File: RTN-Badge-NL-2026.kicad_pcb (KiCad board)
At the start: 2 copper layers, 85.5 x 54 mm, 151 parts, among them J1 USB_A_Edge_Connector, J2 DEBUG, J3 GPIO, SW1 BOOT, SW2 RST, SW3 USER1, SW4 USER2, U1 CH32V203F6P6, U2 XC6206PxxxMR, Y1 8MHz

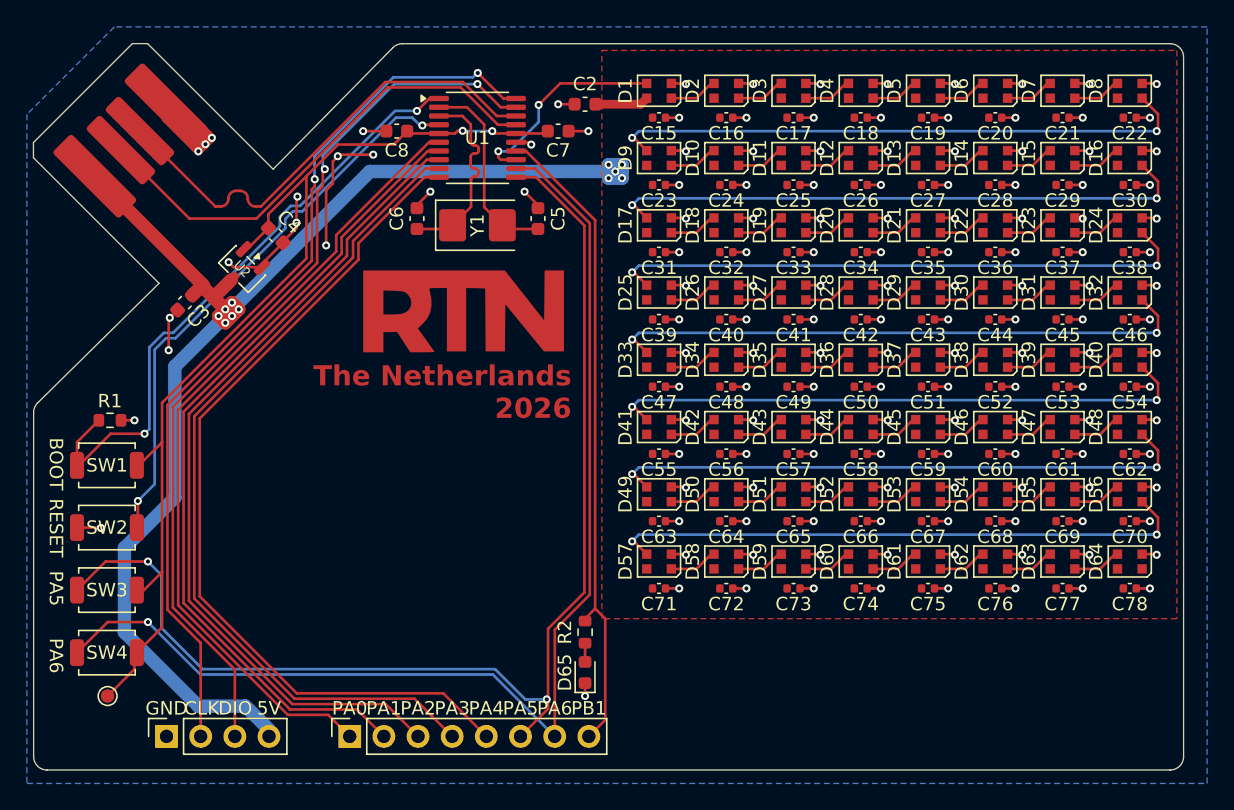
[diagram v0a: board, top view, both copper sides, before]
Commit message: Hide reference designators, clean up traces
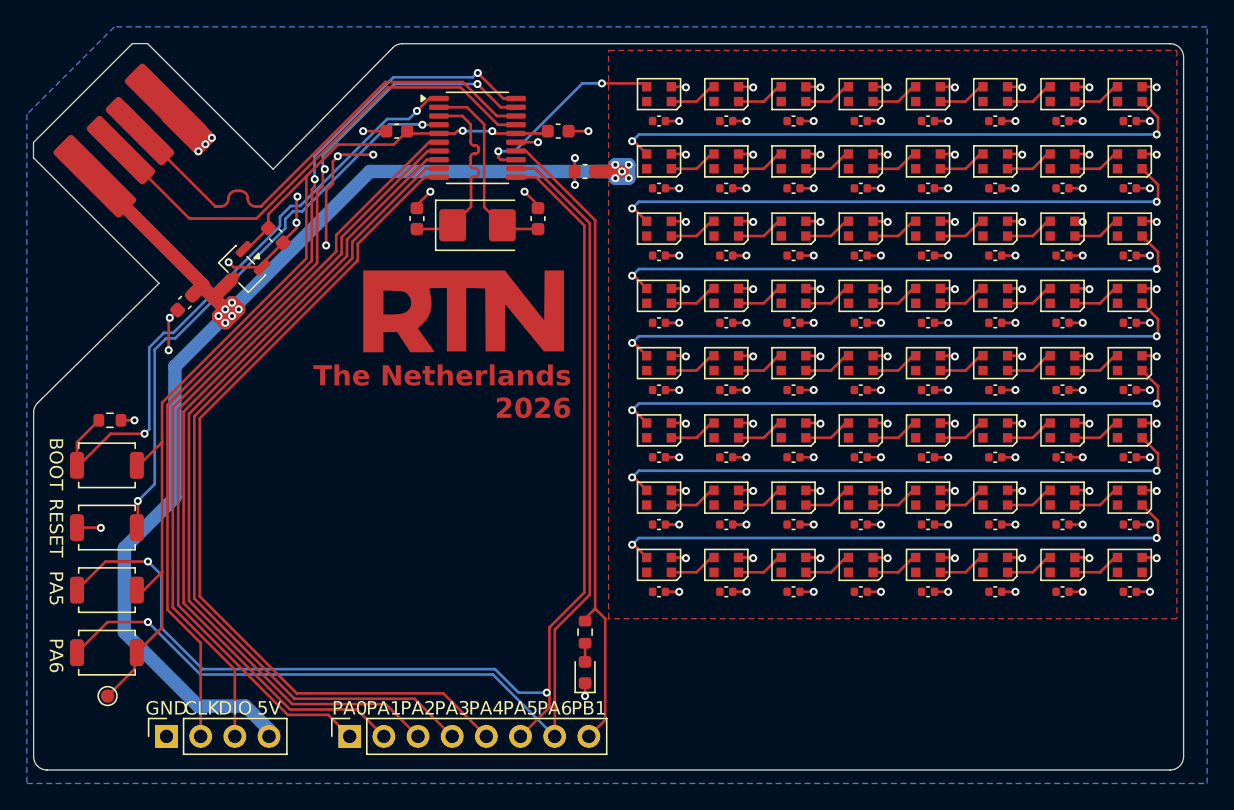
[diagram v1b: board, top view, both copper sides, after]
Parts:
- moved C2 5.00 mm to (66.0, 34.5)
- moved C15 0.25 mm to (71.5, 30.8)
- moved C16 0.25 mm to (76.5, 30.8)
- moved C17 0.25 mm to (81.5, 30.8)
- moved C18 0.25 mm to (86.5, 30.8)
- moved C19 0.25 mm to (91.5, 30.8)
- moved C20 0.25 mm to (96.5, 30.8)
- moved C21 0.25 mm to (101.5, 30.8)
- moved C22 0.25 mm to (106.5, 30.8)
- moved C23 0.25 mm to (71.5, 35.8)
- moved C24 0.25 mm to (76.5, 35.8)
- moved C25 0.25 mm to (81.5, 35.8)
- moved C26 0.25 mm to (86.5, 35.8)
- moved C27 0.25 mm to (91.5, 35.8)
- moved C28 0.25 mm to (96.5, 35.8)
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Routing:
- net +5V: track 103.9 -> 101.9 mm
- net GND: track 193.0 -> 194.3 mm, vias 148 -> 149
- net MATRIX_SPI: track 15.7 -> 15.0 mm

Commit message: Adjust cosmetic text
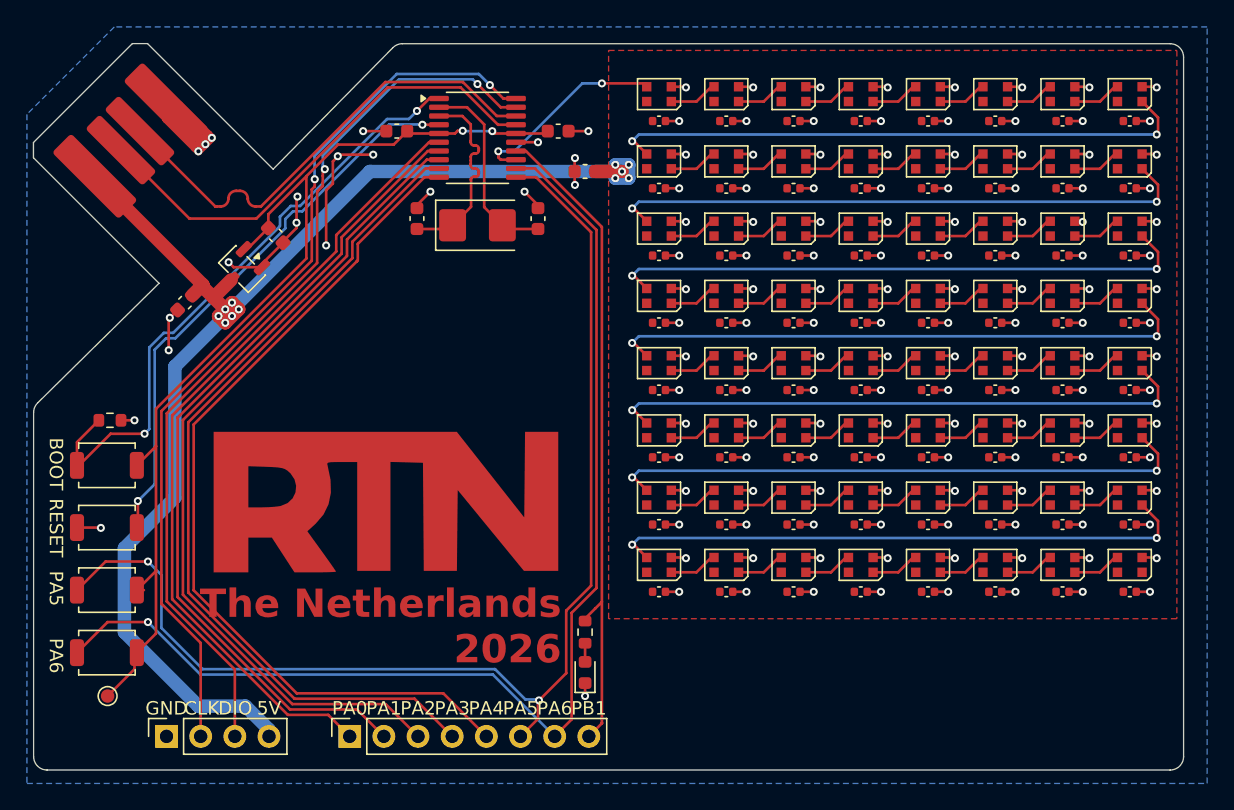
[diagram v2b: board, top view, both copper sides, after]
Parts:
- removed the G*** at (57.0, 45.0) (x2)
- added G*** (x2): LOGO, LOGO, F.Cu at (51.2, 59.2)
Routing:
- net /SWDIO: track 67.1 -> 67.8 mm
- net +3V3: track 76.4 -> 75.8 mm
- net /PB1: track 48.7 -> 49.2 mm
- net /PA5: track 89.3 -> 88.8 mm
